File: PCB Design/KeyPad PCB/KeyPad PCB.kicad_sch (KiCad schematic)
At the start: 1 part

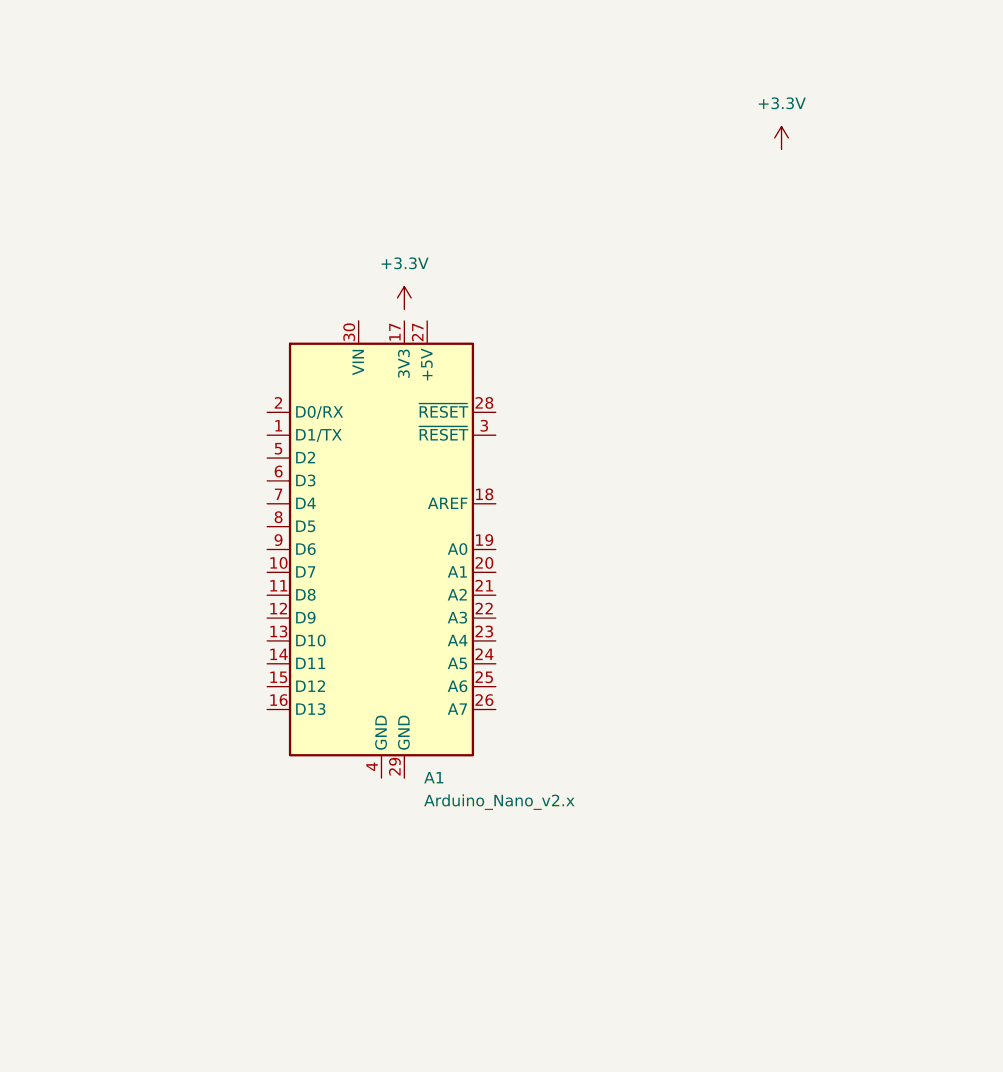
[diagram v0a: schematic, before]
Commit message: Deleted file
inside Knob,Hat ,Swicth folder
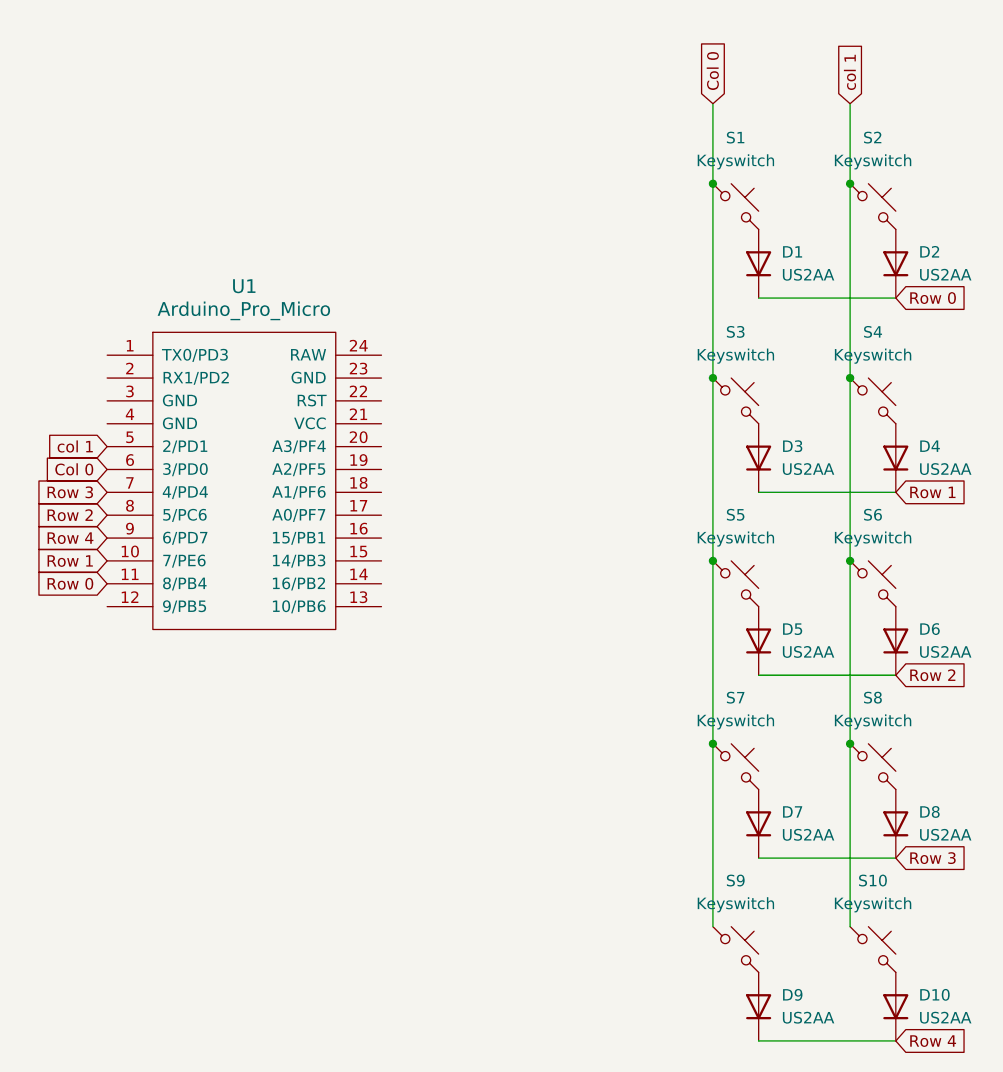
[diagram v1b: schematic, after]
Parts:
- removed A1: Arduino_Nano_v2.x, Module:Arduino_Nano, symbol MCU_Module:Arduino_Nano_v2.x
- added D1, D10, D2, D3, D4, D5, D6, D7, D8, D9: US2AA, ScottoKeebs_Components:Resistor_0805, symbol Diode:US2AA
- added S1, S10, S2, S3, S4, S5, S6, S7, S8, S9: Keyswitch, ScottoKeebs_MX:MX_PCB_1.00u, symbol ScottoKeebs:Placeholder_Keyswitch
- added U1: Arduino_Pro_Micro, ScottoKeebs_MCU:Arduino_Pro_Micro, symbol ScottoKeebs:MCU_Arduino_Pro_Micro
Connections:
- new net: D6.2 (A), S6.2
- new net: D4.2 (A), S4.2
- new net: D5.2 (A), S5.2
- new net: D10.2 (A), S10.2
- new net: D2.2 (A), S2.2
- new net: D1.2 (A), S1.2
- new net: D8.2 (A), S8.2
- new net: D3.2 (A), S3.2
- new net: D9.2 (A), S9.2
- new net: D7.2 (A), S7.2
- new net Col 0: S1.1, S3.1, S5.1, S7.1, S9.1, U1.6 (3/PD0)
- new net Row 0: D1.1 (K), D2.1 (K), U1.11 (8/PB4)
- new net Row 1: D3.1 (K), D4.1 (K), U1.10 (7/PE6)
- new net Row 2: D5.1 (K), D6.1 (K), U1.8 (5/PC6)
- new net Row 3: D7.1 (K), D8.1 (K), U1.7 (4/PD4)
- new net Row 4: D10.1 (K), D9.1 (K), U1.9 (6/PD7)
- new net col 1: S10.1, S2.1, S4.1, S6.1, S8.1, U1.5 (2/PD1)
